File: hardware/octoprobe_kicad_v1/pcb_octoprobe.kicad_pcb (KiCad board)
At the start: 2 copper layers, 100 x 160 mm, 602 parts, among them J101 Conn_01x20, J102 Conn_01x20, J103 Conn_01x20, J104 Conn_01x20, J105 Conn_01x20, J201 USB_C_Receptacle_USB2.0, J202 BOOT cap enable, J203 BOOT Button, J204 BOOT cap 2, SW202 RESET, U201 RP2040, U202 AMS1117-3.3, U203 W25Q128JVS, U301 GAQY221S, U401 GAQY221S, U501 GAQY221S, U601 GAQY221S, U701 GAQY221S, Y201 Crystal_GND24_Small

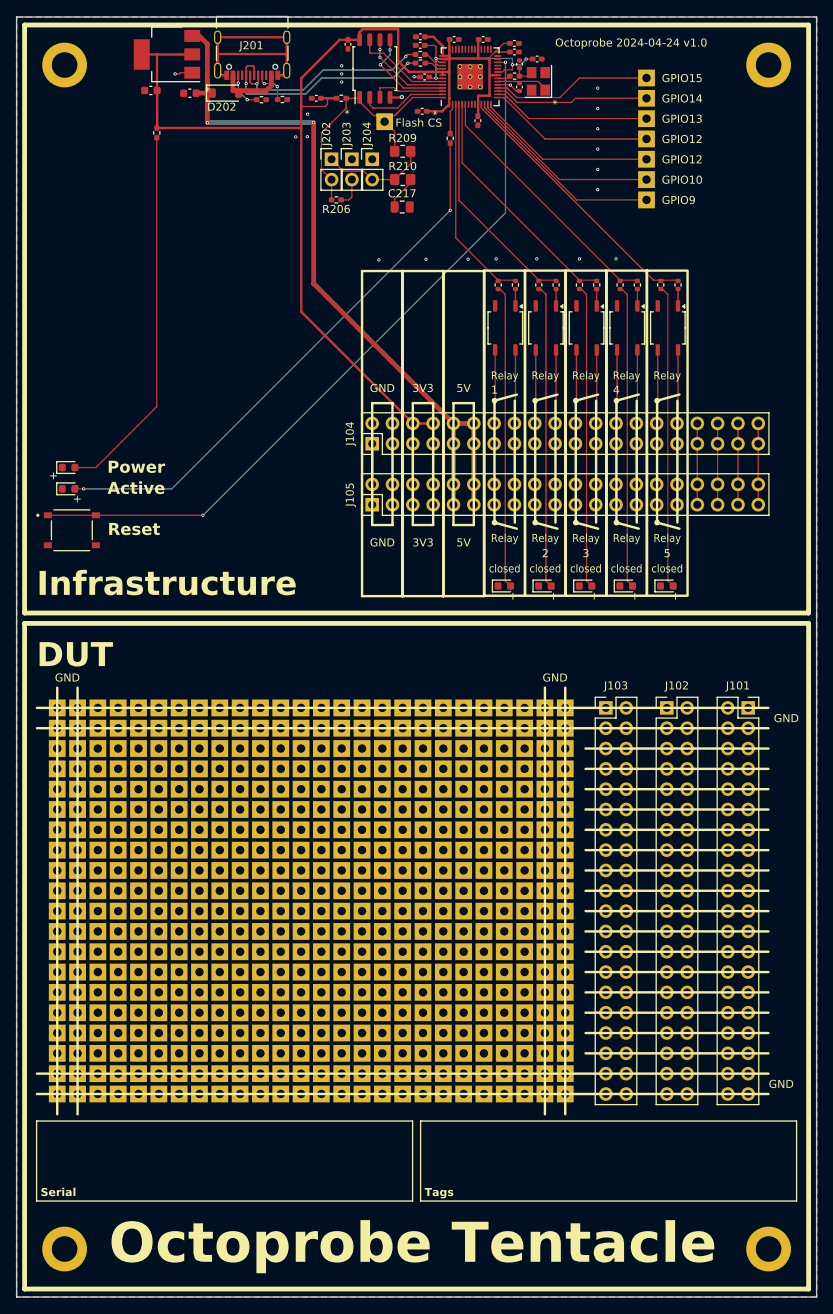
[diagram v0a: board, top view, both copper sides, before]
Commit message: Add 5V 500mA
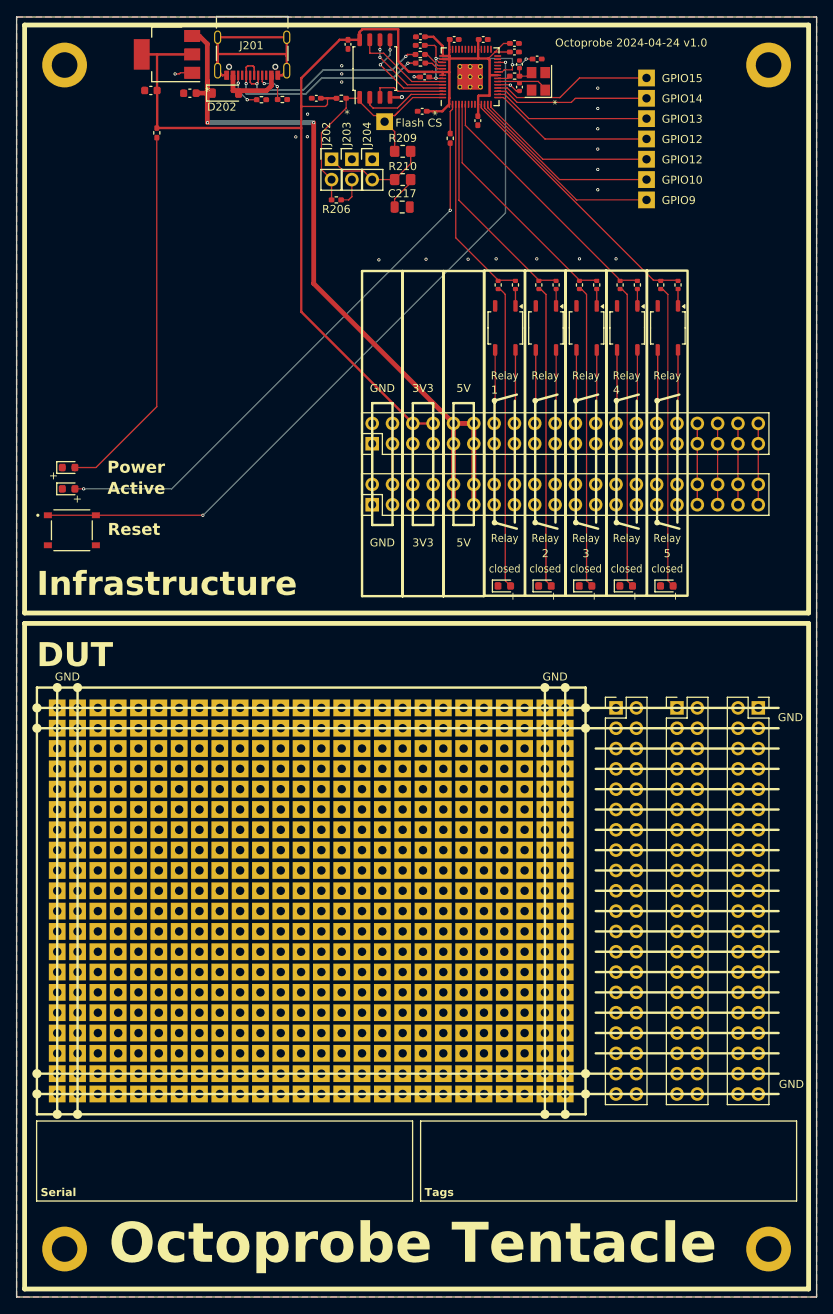
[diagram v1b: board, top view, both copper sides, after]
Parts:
- moved J101 1.27 mm to (166.7, 118.9)
- moved J102 1.27 mm to (159.1, 118.9)
- moved J103 1.27 mm to (151.5, 118.9)

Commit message: Cable Tie
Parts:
- added H105: octoprobe_CableTieHole, 00_project_library:octoprobe_CableTieHole, F.Cu at (77.8, 49.0)
- added H106: octoprobe_CableTieHole, 00_project_library:octoprobe_CableTieHole, F.Cu at (84.2, 49.0)
- added H107: octoprobe_CableTieHole, 00_project_library:octoprobe_CableTieHole, F.Cu at (77.8, 96.0)
- added H108: octoprobe_CableTieHole, 00_project_library:octoprobe_CableTieHole, F.Cu at (84.2, 96.0)
- moved D101 11.2 mm to (91.6, 90.4)
- moved D201 11.2 mm to (91.6, 87.7)
- moved SW202 10.9 mm to (91.7, 95.8)
- moved R201 0.89 mm to (92.4, 47.0)
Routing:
- net Net-(D101-A): track 69.7 -> 57.7 mm
- net Net-(D201-A): track 47.0 -> 40.1 mm
- net Net-(U201-RUN): track 79.3 -> 81.0 mm
- net +3V3: track 177.0 -> 176.4 mm

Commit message: PCB octoprobe tentacle v1.0
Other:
- board text added: "tentacle"
- board text removed: "Octoprobe Tentacle"
